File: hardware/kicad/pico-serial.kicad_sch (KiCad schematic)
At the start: 81 parts, among them J1 USB_C, J2 DB25_Female, SW1 BOOTSEL, SW2 RESET, U1 RP2040, U2 W25Q128JVS, U3 AP2112K-3.3, U4 USBLC6-2SC6, U5 SP3238EEA, U6 MAX3243EIDBR, Y1 12MHz

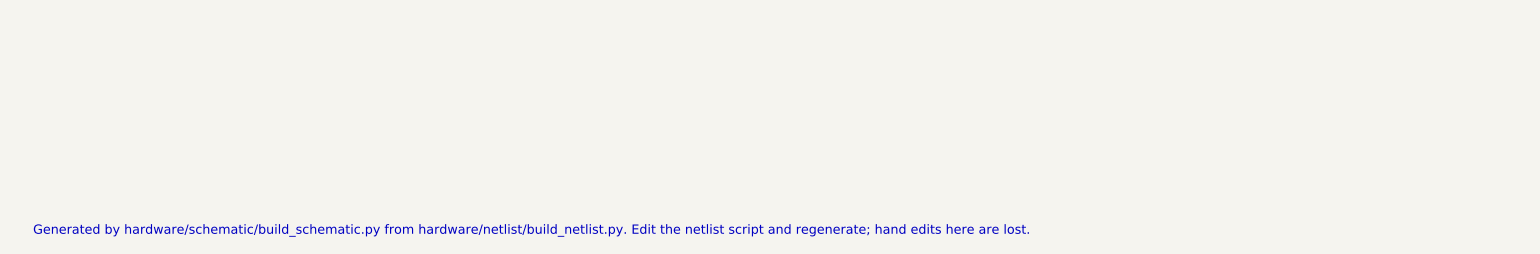
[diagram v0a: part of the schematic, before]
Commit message: Hardware: start the PCB (placed, not yet routed)
- hardware/schematic -> hardware/kicad, so the schematic and PCB are one
  KiCad project.
- kicad/build_pcb.py lays out the board from the netlist script with
  KiCad 9's Python module: outline (SPEC 7.2, inferred), JLC 4-layer
  rules and net classes, footprints linked to their schematic symbols,
  placement on both sides, a GND plane on In1, a via for every GND and
  +3V3 pad, silkscreen (licence and Source Location), and optional
  autorouting with Freerouting and fab outputs.
- kicad/pico-serial.kicad_dru: edge rules for the DB25 cups and USB-C.
- The committed board is placed but unrouted; routing comes next.

Co-Authored-By: Claude Opus 5.5 <noreply@anthropic.com>
Claude-Session: https://claude.ai/code/session_013PRsUCpxazyipPn5UGGkF8
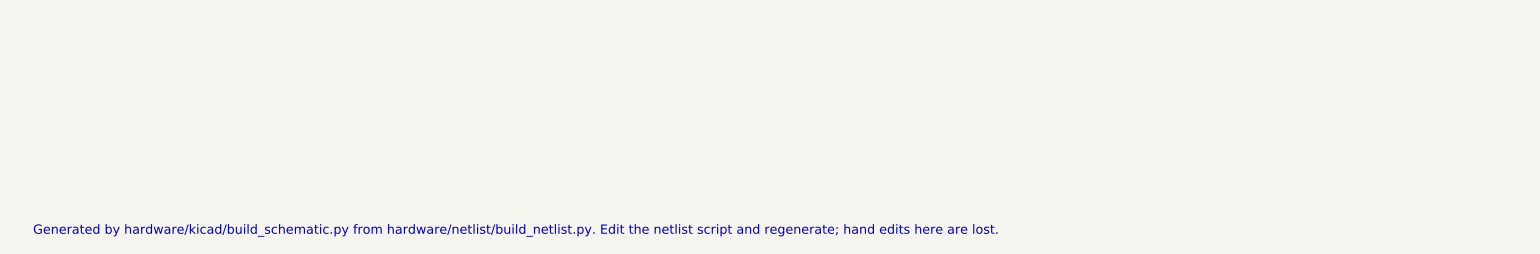
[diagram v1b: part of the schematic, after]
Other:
- note added: "Generated by hardware/kicad/build_schematic.py from hardware/netlist/build_netlist.py. Edit the netlist script and regenerate; hand edits here are lost."
- note removed: "Generated by hardware/schematic/build_schematic.py from hardware/netlist/build_netlist.py. Edit the netlist script and regenerate; hand edits here are lost."
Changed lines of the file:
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@@
 		(effects (font (size 2 2) (bold yes)) (justify left bottom))
 	)
-	(text "Generated by hardware/schematic/build_schematic.py from hardware/netlist/build_netlist.py. Edit the netlist script and regenerate; hand edits here are lost."
+	(text "Generated by hardware/kicad/build_schematic.py from hardware/netlist/build_netlist.py. Edit the netlist script and regenerate; hand edits here are lost."
 		(exclude_from_sim no)
 		(at 20.32 407.3 0)
